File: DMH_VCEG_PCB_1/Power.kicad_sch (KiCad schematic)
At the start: 54 parts, among them J0 Conn_01x01, J100 IDC_02x08, U1 TL074, U10 TL074, U11 4001, U12 40106, U13 CD4066BE, U14 TL074, U15 TL074, U16 TL074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

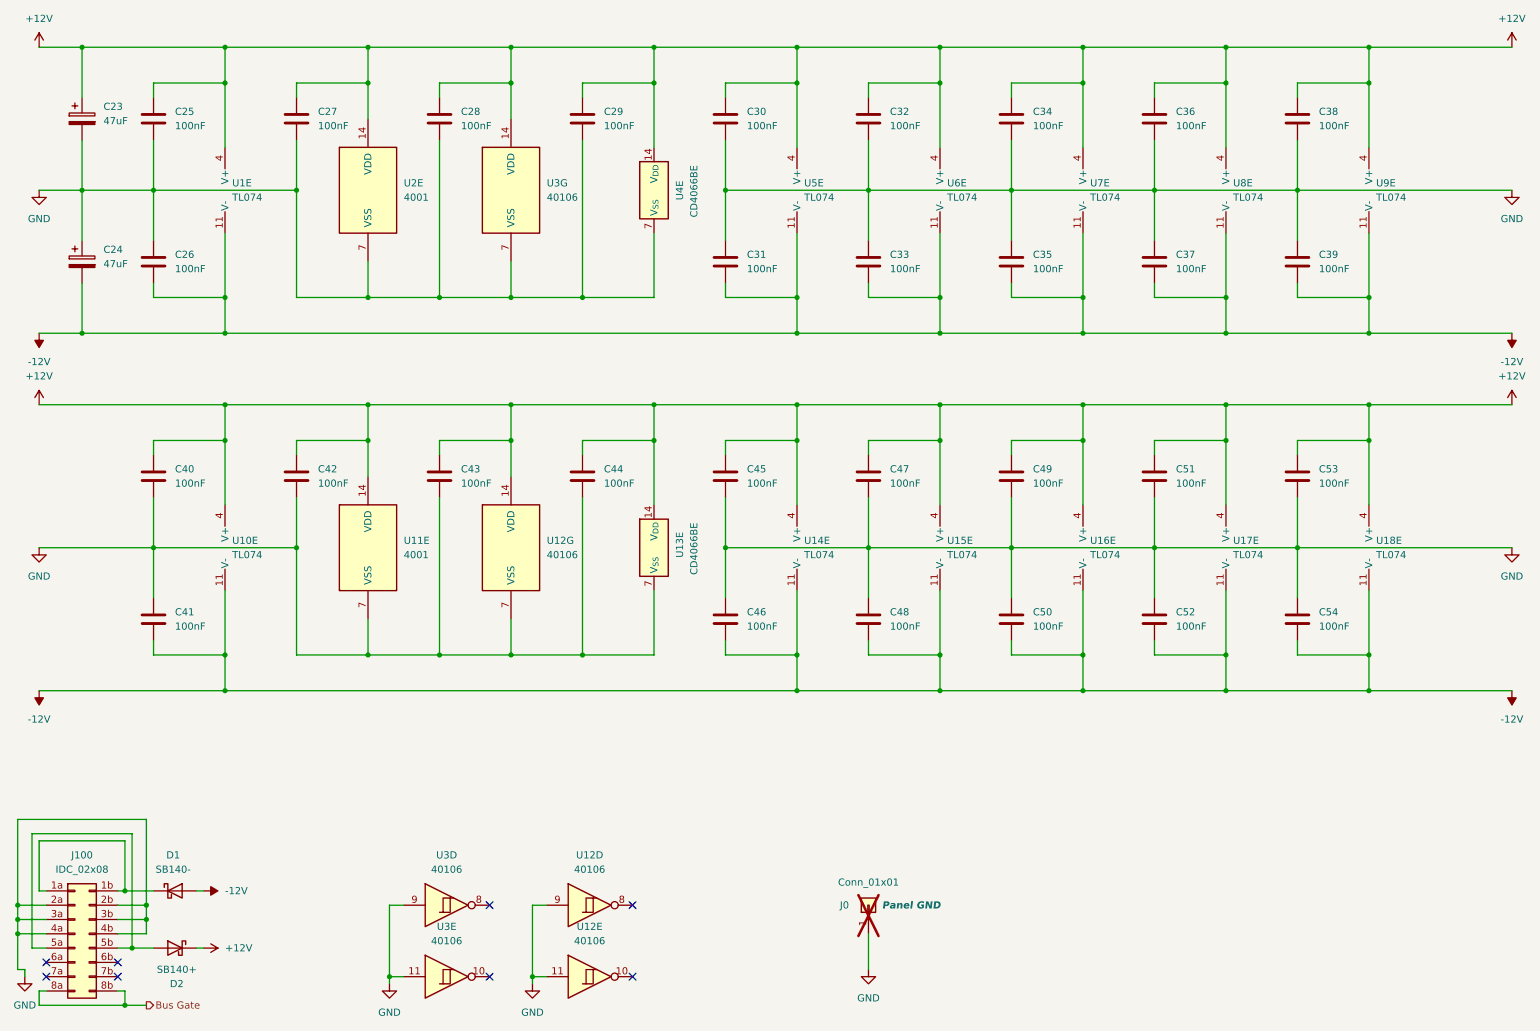
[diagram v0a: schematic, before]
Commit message: Updated SG Out circuit
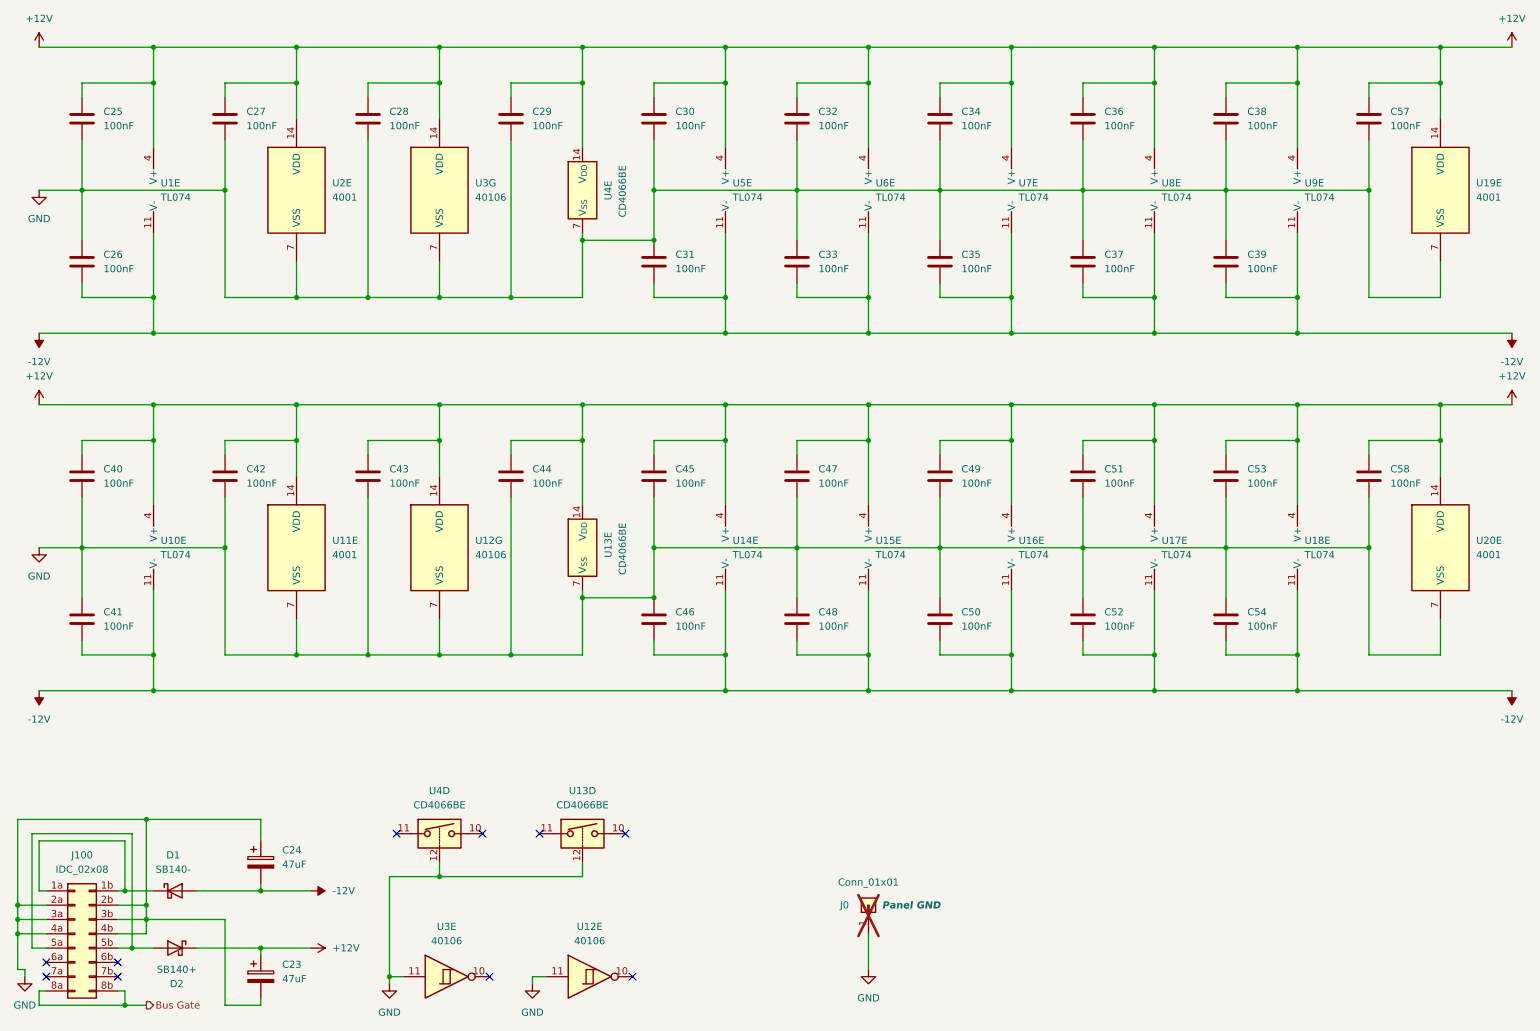
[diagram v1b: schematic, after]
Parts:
- removed unit 4 of U12
- removed unit 4 of U3
- added C57, C58: 100nF, Capacitor_THT:C_Disc_D4.3mm_W1.9mm_P5.00mm, symbol Device:C
- added unit 4 of U13
- added U19, U20: 4001, Package_DIP:DIP-14_W7.62mm_Socket, symbol 4xxx:4001
- added unit 4 of U4
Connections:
- net +12V: now also C57.1, C58.1, U19.14 (VDD), U20.14 (VDD)
- net GND: now also C57.2, C58.2, U13.12, U19.7 (VSS), U20.7 (VSS), U4.12
- no-connect marks 8 -> 10
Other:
- moved on the sheet: C23, C24, C25, C26, C27, C28, C29, C30, C31, C32, C33, C34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

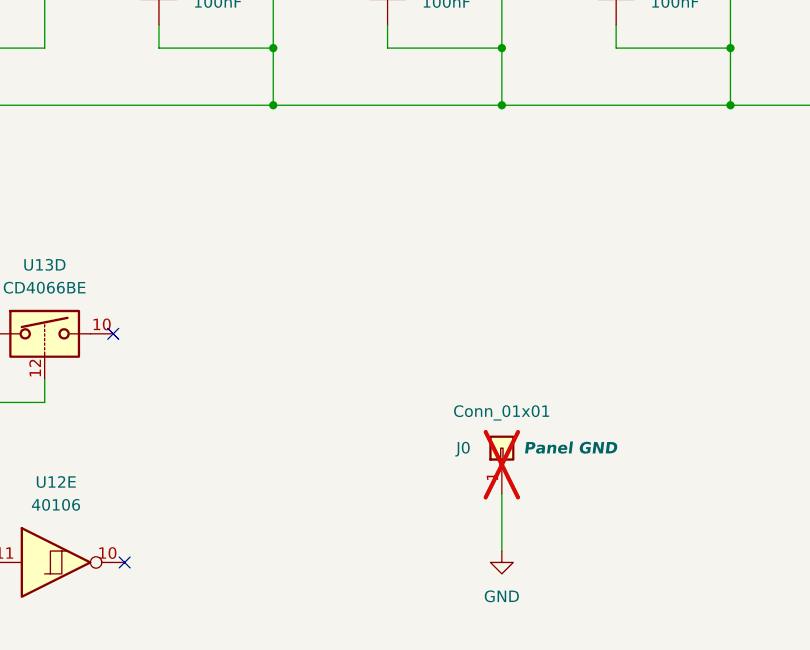
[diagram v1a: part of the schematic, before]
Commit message: Added Loop circuit
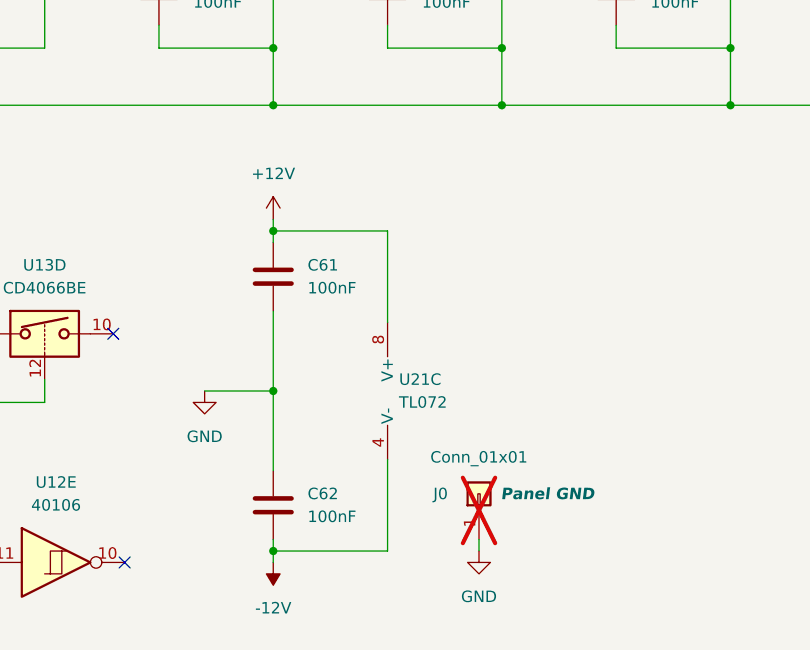
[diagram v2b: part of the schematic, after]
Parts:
- added C61, C62: 100nF, Capacitor_THT:C_Disc_D4.3mm_W1.9mm_P5.00mm, symbol Device:C
- added U21: TL072, symbol Amplifier_Operational:TL072
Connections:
- net +12V: now also C61.1, U21.8 (V+)
- net -12V: now also C62.2, U21.4 (V-)
- net GND: now also C61.2, C62.1
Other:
- moved on the sheet: J0

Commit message: PCB 1 ready for placement
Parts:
- U21: footprint (none) -> Package_DIP:DIP-8_W7.62mm
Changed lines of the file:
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@@
 		(exclude_from_sim no)
 		(in_bom yes)
-		(on_board yes)
+		(on_board no)
 		(dnp no)
 		(fields_autoplaced yes)
@@
 		(exclude_from_sim no)
 		(in_bom yes)
-		(on_board yes)
+		(on_board no)
 		(dnp no)
 		(fields_autoplaced yes)
@@
 		(exclude_from_sim no)
 		(in_bom yes)
-		(on_board yes)
+		(on_board no)
 		(dnp no)
 		(fields_autoplaced yes)
@@
 		(exclude_from_sim no)
 		(in_bom yes)
-		(on_board yes)
+		(on_board no)
 		(dnp no)
 		(fields_autoplaced yes)
@@
 		(exclude_from_sim no)
 		(in_bom yes)
-		(on_board yes)
+		(on_board no)
 		(dnp no)
 		(fields_autoplaced yes)
@@
 		(exclude_from_sim no)
 		(in_bom yes)
-		(on_board yes)
+		(on_board no)
 		(dnp no)
 		(fields_autoplaced yes)
@@
 		(exclude_from_sim no)
 		(in_bom yes)
-		(on_board yes)
+		(on_board no)
 		(dnp no)
 		(fields_autoplaced yes)
@@
 		(exclude_from_sim no)
 		(in_bom yes)
-		(on_board yes)
+		(on_board no)
 		(dnp no)
 		(fields_autoplaced yes)
@@
 		(exclude_from_sim no)
 		(in_bom yes)
-		(on_board yes)
+		(on_board no)
 		(dnp no)
 		(fields_autoplaced yes)
@@
 		(exclude_from_sim no)
 		(in_bom yes)
-		(on_board yes)
+		(on_board no)
 		(dnp no)
 		(fields_autoplaced yes)
@@
 		(exclude_from_sim no)
 		(in_bom yes)
-		(on_board yes)
+		(on_board no)
 		(dnp no)
 		(fields_autoplaced yes)
@@
 		(exclude_from_sim no)
 		(in_bom yes)
-		(on_board yes)
+		(on_board no)
 		(dnp no)
 		(fields_autoplaced yes)
@@
 		(exclude_from_sim no)
 		(in_bom yes)
-		(on_board yes)
+		(on_board no)
 		(dnp no)
 		(fields_autoplaced yes)
@@
 			)
 		)
-		(property "Footprint" ""
+		(property "Footprint" "Package_DIP:DIP-8_W7.62mm"
 			(at 154.94 171.45 0)
 			(effects
@@
 		(exclude_from_sim no)
 		(in_bom yes)
-		(on_board yes)
+		(on_board no)
 		(dnp no)
 		(fields_autoplaced yes)
@@
 		(exclude_from_sim no)
 		(in_bom yes)
-		(on_board yes)
+		(on_board no)
 		(dnp no)
 		(fields_autoplaced yes)
@@
 		(exclude_from_sim no)
 		(in_bom yes)
-		(on_board yes)
+		(on_board no)
 		(dnp no)
 		(fields_autoplaced yes)
@@
 		(exclude_from_sim no)
 		(in_bom yes)
-		(on_board yes)
+		(on_board no)
 		(dnp no)
 		(fields_autoplaced yes)
@@
 		(exclude_from_sim no)
 		(in_bom yes)
-		(on_board yes)
+		(on_board no)
 		(dnp no)
 		(fields_autoplaced yes)
@@
 		(exclude_from_sim no)
 		(in_bom yes)
-		(on_board yes)
+		(on_board no)
 		(dnp no)
 		(fields_autoplaced yes)
@@
 		(exclude_from_sim no)
 		(in_bom yes)
-		(on_board yes)
+		(on_board no)
 		(dnp no)
 		(fields_autoplaced yes)
@@
 		(exclude_from_sim no)
 		(in_bom yes)
-		(on_board yes)
+		(on_board no)
 		(dnp no)
 		(fields_autoplaced yes)

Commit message: Placed ICs and pin headers on PCB 2
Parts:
- removed J0: Conn_01x01, Connector_PinHeader_2.54mm:PinHeader_1x01_P2.54mm_Vertical, symbol Connector_Generic:Conn_01x01
- U21: footprint Package_DIP:DIP-8_W7.62mm -> Package_DIP:DIP-8_W7.62mm_Socket
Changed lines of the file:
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@@
 	(wire
 		(pts
-			(xy 162.56 187.96) (xy 162.56 189.23)
-		)
-		(stroke
-			(width 0)
-			(type default)
-		)
-	)
-	(wire
-		(pts
 			(xy 241.3 58.42) (xy 241.3 69.85)
 		)
@@
 	)
 	(symbol
-		(lib_id "power:GND")
-		(at 162.56 189.23 0)
-		(unit 1)
-		(exclude_from_sim no)
-		(in_bom yes)
-		(on_board yes)
-		(dnp no)
-		(fields_autoplaced yes)
-		(property "Reference" "#PWR0118"
-			(at 162.56 195.58 0)
-			(effects
-				(font
-					(size 1.27 1.27)
-				)
-				(hide yes)
-			)
-		)
-		(property "Value" "GND"
-			(at 162.56 194.31 0)
-			(effects
-				(font
-					(size 1.27 1.27)
-				)
-			)
-		)
-		(property "Footprint" ""
-			(at 162.56 189.23 0)
-			(effects
-				(font
-					(size 1.27 1.27)
-				)
-				(hide yes)
-			)
-		)
-		(property "Datasheet" ""
-			(at 162.56 189.23 0)
-			(effects
-				(font
-					(size 1.27 1.27)
-				)
-				(hide yes)
-			)
-		)
-		(property "Description" "Power symbol creates a global label with name \"GND\" , ground"
-			(at 162.56 189.23 0)
-			(effects
-				(font
-					(size 1.27 1.27)
-				)
-				(hide yes)
-			)
-		)
-		(pin "1"
-		)
-		(instances
-			(project "DMH-Kosmo-10cm-PCB"
-				(path "/58f4306d-5387-4983-bb08-41a2313fd315/0cdf34b2-39cd-4d9e-981a-97cd34791509"
-					(reference "#PWR0118")
-					(unit 1)
-				)
-			)
-		)
-	)
-	(symbol
 		(lib_id "4xxx:4001")
 		(at 266.7 114.3 0)
@@
 	)
 	(symbol
-		(lib_id "Connector_Generic:Conn_01x01")
-		(at 162.56 182.88 90)
-		(unit 1)
-		(exclude_from_sim no)
-		(in_bom no)
-		(on_board no)
-		(dnp yes)
-		(property "Reference" "J0"
-			(at 157.48 182.88 90)
-			(effects
-				(font
-					(size 1.27 1.27)
-				)
-				(justify right)
-			)
-		)
-		(property "Value" "Conn_01x01"
-			(at 162.56 178.816 90)
-			(effects
-				(font
-					(size 1.27 1.27)
-				)
-			)
-		)
-		(property "Footprint" "Connector_PinHeader_2.54mm:PinHeader_1x01_P2.54mm_Vertical"
-			(at 162.56 182.88 0)
-			(effects
-				(font
-					(size 1.27 1.27)
-				)
-				(hide yes)
-			)
-		)
-		(property "Datasheet" "~"
-			(at 162.56 182.88 0)
-			(effects
-				(font
-					(size 1.27 1.27)
-				)
-				(hide yes)
-			)
-		)
-		(property "Description" "Generic connector, single row, 01x01, script generated (kicad-library-utils/schlib/autogen/connector/)"
-			(at 162.56 182.88 0)
-			(effects
-				(font
-					(size 1.27 1.27)
-				)
-				(hide yes)
-			)
-		)
-		(property "Function" "Panel GND"
-			(at 170.18 182.88 90)
-			(effects
-				(font
-					(size 1.27 1.27)
-					(thickness 0.254)
-					(bold yes)
-					(italic yes)
-				)
-			)
-		)
-		(pin "1"
-		)
-		(instances
-			(project "DMH-Kosmo-10cm-PCB"
-				(path "/58f4306d-5387-4983-bb08-41a2313fd315/0cdf34b2-39cd-4d9e-981a-97cd34791509"
-					(reference "J0")
-					(unit 1)
-				)
-			)
-		)
-	)
-	(symbol
 		(lib_id "Device:C")
 		(at 177.8 101.6 0)
@@
 		(exclude_from_sim no)
 		(in_bom yes)
-		(on_board no)
+		(on_board yes)
 		(dnp no)
 		(fields_autoplaced yes)
@@
 			)
 		)
-		(property "Footprint" "Package_DIP:DIP-8_W7.62mm"
+		(property "Footprint" "Package_DIP:DIP-8_W7.62mm_Socket"
 			(at 154.94 171.45 0)
 			(effects
@@
 			)
 		)
+		(property "Function" ""
+			(at 154.94 171.45 0)
+			(effects
+				(font
+					(size 1.27 1.27)
+				)
+			)
+		)
 		(pin "4"
 		)
@@
 		(exclude_from_sim no)
 		(in_bom yes)
-		(on_board no)
+		(on_board yes)
 		(dnp no)
 		(fields_autoplaced yes)

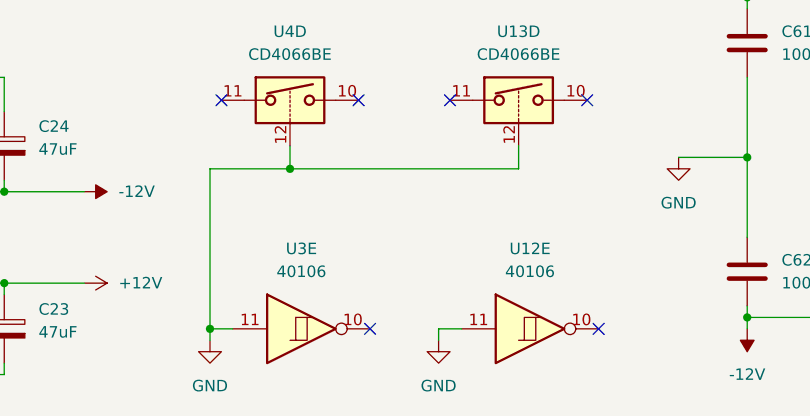
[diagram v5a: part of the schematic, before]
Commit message: Copied Manual Gate circuit to PCB 1 schematic
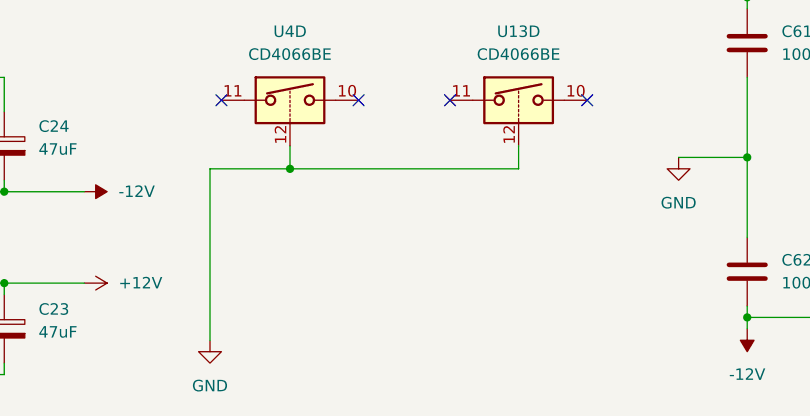
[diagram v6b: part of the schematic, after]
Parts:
- removed unit 5 of U12
- removed unit 5 of U3
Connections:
- no-connect marks 10 -> 8

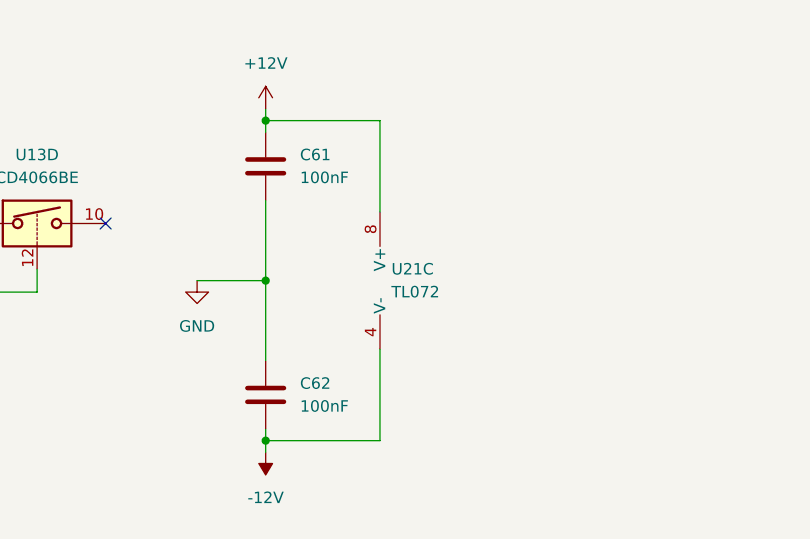
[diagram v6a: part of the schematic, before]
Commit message: Added Output attenuation circuit
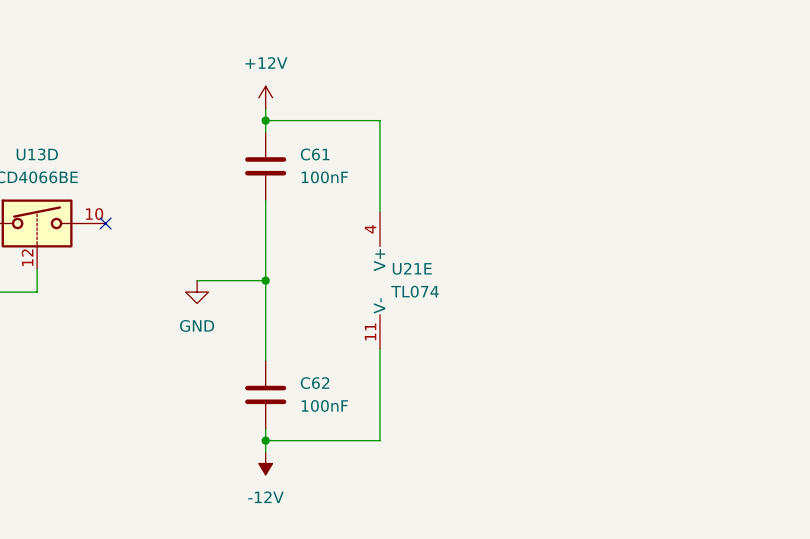
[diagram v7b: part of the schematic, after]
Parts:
- removed U21: TL072, Package_DIP:DIP-8_W7.62mm_Socket, symbol Amplifier_Operational:TL072
- added U21: TL074, symbol Amplifier_Operational:TL074
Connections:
- net +12V: now also U21.4 (V+)
- net -12V: now also U21.11 (V-)
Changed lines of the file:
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@@
-	)
-	(symbol
-		(lib_id "Amplifier_Operational:TL072")
-		(at 154.94 171.45 0)
-		(unit 3)
-		(exclude_from_sim no)
-		(in_bom yes)
-		(on_board no)
-		(dnp no)
-		(fields_autoplaced yes)
-		(property "Reference" "U21"
-			(at 153.67 170.1799 0)
-			(effects
-				(font
-					(size 1.27 1.27)
-				)
-				(justify left)
-			)
-		)
-		(property "Value" "TL072"
-			(at 153.67 172.7199 0)
-			(effects
-				(font
-					(size 1.27 1.27)
-				)
-				(justify left)
-			)
-		)
-		(property "Footprint" "Package_DIP:DIP-8_W7.62mm_Socket"
-			(at 154.94 171.45 0)
-			(effects
-				(font
-					(size 1.27 1.27)
-				)
-				(hide yes)
-			)
-		)
-		(property "Datasheet" "http://www.ti.com/lit/ds/symlink/tl071.pdf"
-			(at 154.94 171.45 0)
-			(effects
-				(font
-					(size 1.27 1.27)
-				)
-				(hide yes)
-			)
-		)
-		(property "Description" "Dual Low-Noise JFET-Input Operational Amplifiers, DIP-8/SOIC-8"
-			(at 154.94 171.45 0)
-			(effects
-				(font
-					(size 1.27 1.27)
-				)
-				(hide yes)
-			)
-		)
-		(property "Function" ""
-			(at 154.94 171.45 0)
-			(effects
-				(font
-					(size 1.27 1.27)
-				)
-			)
-		)
-		(pin "4"
-		)
-		(pin "2"
-		)
-		(pin "7"
-		)
-		(pin "8"
-		)
-		(pin "1"
-		)
-		(pin "6"
-		)
-		(pin "3"
-		)
-		(pin "5"
-		)
-		(instances
-			(project ""
-				(path "/58f4306d-5387-4983-bb08-41a2313fd315/0cdf34b2-39cd-4d9e-981a-97cd34791509"
-					(reference "U21")
-					(unit 3)
-				)
-			)
-		)
 	)
 	(symbol
@@
 					(unit 5)
 				)
+			)
+		)
+	)
+	(symbol
+		(lib_id "Amplifier_Operational:TL074")
+		(at 154.94 171.45 0)
+		(unit 5)
+		(exclude_from_sim no)
+		(in_bom yes)
+		(on_board no)
+		(dnp no)
+		(fields_autoplaced yes)
+		(property "Reference" "U21"
+			(at 153.67 170.1799 0)
+			(effects
+				(font
+					(size 1.27 1.27)
+				)
+				(justify left)
+			)
+		)
+		(property "Value" "TL074"
+			(at 153.67 172.7199 0)
+			(effects
+				(font
+					(size 1.27 1.27)
+				)
+				(justify left)
+			)
+		)
+		(property "Footprint" ""
+			(at 153.67 168.91 0)
+			(effects
+				(font
+					(size 1.27 1.27)
+				)
+				(hide yes)
+			)
+		)
+		(property "Datasheet" "http://www.ti.com/lit/ds/symlink/tl071.pdf"
+			(at 156.21 166.37 0)
+			(effects
+				(font
+					(size 1.27 1.27)
+				)
+				(hide yes)
+			)
+		)
+		(property "Description" "Quad Low-Noise JFET-Input Operational Amplifiers, DIP-14/SOIC-14"
+			(at 154.94 171.45 0)
+			(effects
+				(font
+					(size 1.27 1.27)
+				)
+				(hide yes)
+			)
+		)
+		(pin "11"
+		)
+		(pin "9"
+		)
+		(pin "3"
+		)
+		(pin "10"
+		)
+		(pin "7"
+		)
+		(pin "5"
+		)
+		(pin "2"
+		)
+		(pin "8"
+		)
+		(pin "1"
+		)
+		(pin "6"
+		)
+		(pin "12"
+		)
+		(pin "13"
+		)
+		(pin "14"
+		)
+		(pin "4"
+		)
+		(instances
+			(project ""
+				(path "/58f4306d-5387-4983-bb08-41a2313fd315/0cdf34b2-39cd-4d9e-981a-97cd34791509"
+					(reference "U21")
+					(unit 5)
+				)
